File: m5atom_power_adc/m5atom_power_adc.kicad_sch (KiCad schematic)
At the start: 47 parts, among them J1 USB_C_Receptacle_USB2.0_14P, U1 LM2596S-5, U2 ESP32-S3-MINI-1, U3 AMS1117-3.3, U4 ADS1115IDGS, U5 AMS1117-3.3

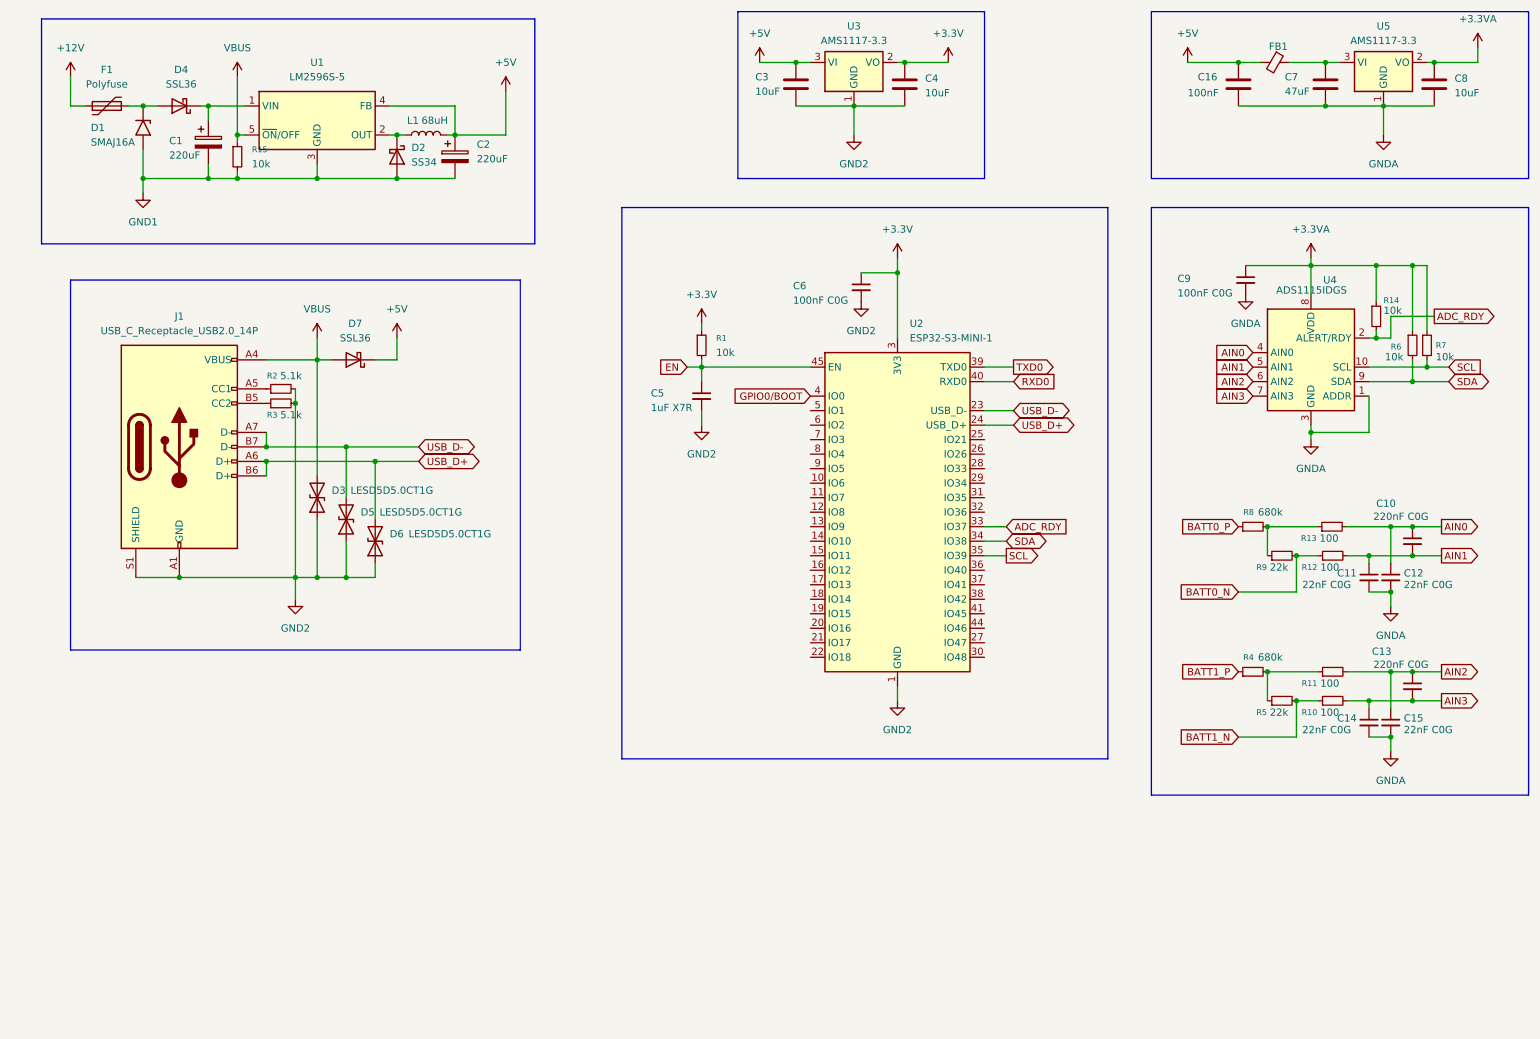
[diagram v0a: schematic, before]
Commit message: fix: 必須な外部接続系を追加
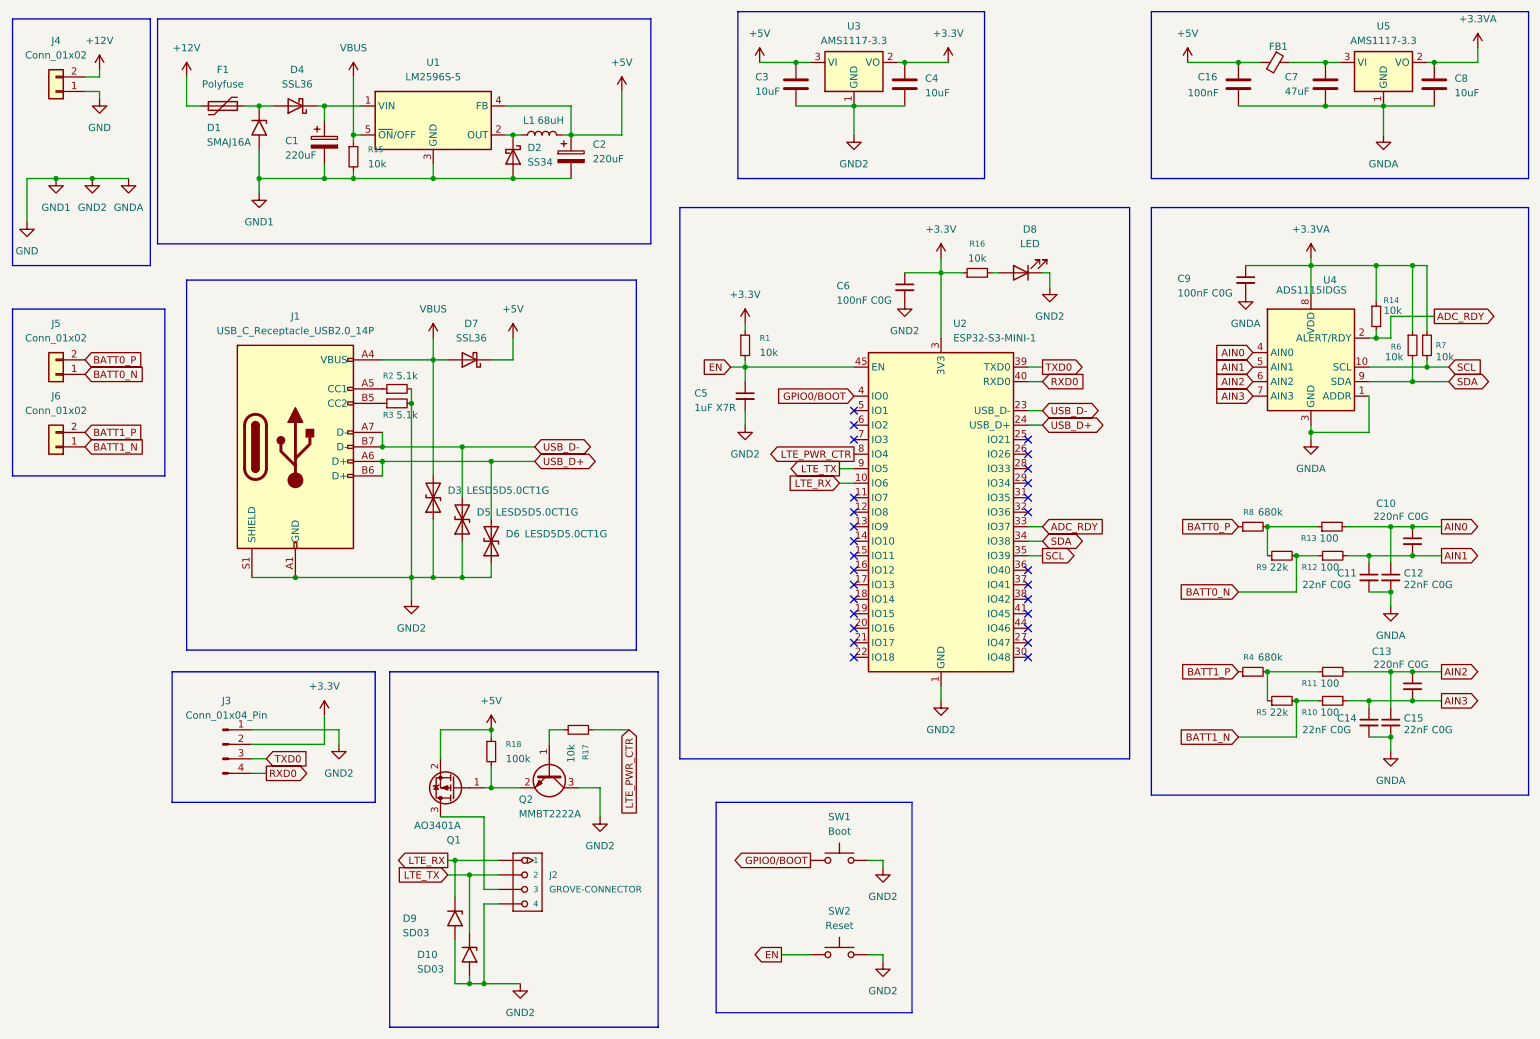
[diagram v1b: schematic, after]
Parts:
- added D10, D9: SD03, Diode_SMD:D_SMA, symbol Diode:SMAJ16A
- added D8: LED, symbol Device:LED
- added J2: GROVE-CONNECTOR, symbol OPL_Connector:GROVE-CONNECTOR-DIP_4P-2.0_
- added J3: Conn_01x04_Pin, symbol Connector:Conn_01x04_Pin
- added J4, J5, J6: Conn_01x02, symbol Connector_Generic:Conn_01x02
- added Q1: AO3401A, Package_TO_SOT_SMD:SOT-23, symbol Transistor_FET:AO3401A
- added Q2: MMBT2222A, Package_TO_SOT_SMD:SOT-23, symbol Transistor_BJT:MMBT2222A
- added R16, R17: 10k, symbol Device:R_Small
- added R18: 100k, symbol Device:R_Small
- added SW1: Boot, symbol Switch:SW_Push
- added SW2: Reset, symbol Switch:SW_Push
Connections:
- net GND2 is gone; now on net GND: C3.2, C4.2, C5.2, C6.2, D3.1 (A1), D5.1 (A1), D6.1 (A1), J1.A1 (GND), J1.A12 (GND), J1.B1 (GND), J1.B12 (GND), J1.S1 (SHIELD), R2.2, R3.2, U2.1 (GND), U2.2 (GND), U2.42 (GND), U2.43 (GND), U2.46 (GND), U2.47 (GND), U2.48 (GND), U2.49 (GND), U2.50 (GND), U2.51 (GND), U2.52 (GND), U2.53 (GND), U2.54 (GND), U2.55 (GND), U2.56 (GND), U2.57 (GND), U2.58 (GND), U2.59 (GND), U2.60 (GND), U2.61 (GND), U2.62 (GND), U2.63 (GND), U2.64 (GND), U2.65 (GND), U3.1 (GND)
- net GNDA is gone; now on net GND: C11.2, C12.2, C14.2, C15.2, C16.2, C7.2, C8.2, C9.2, U4.1 (ADDR), U4.3 (GND), U5.1 (GND)
- net +12V: now also J4.2 (Pin_2)
- net +3.3V: now also J3.2 (Pin_2), R16.1
- net +5V: now also Q1.2 (S), R18.1
- net BATT0_N: now also J5.1 (Pin_1)
- net BATT0_P: now also J5.2 (Pin_2)
- net BATT1_N: now also J6.1 (Pin_1)
- net BATT1_P: now also J6.2 (Pin_2)
- net EN: now also SW2.1
- net GPIO0/BOOT: now also SW1.1
- net RXD0: now also J3.4 (Pin_4)
- net TXD0: now also J3.3 (Pin_3)
- net LTE_RX: now reaches U2.10 (IO6)
- net LTE_RX: now also D9.1 (A1), J2.1
- net LTE_PWR_CTR: now reaches U2.8 (IO4)
- net LTE_PWR_CTR: now also R17.1
- net LTE_TX: now reaches U2.9 (IO5)
- net LTE_TX: now also D10.1 (A1), J2.2
- net GND1 renamed GND
- net GND: now also D10.2 (A2), D8.1 (K), D9.2 (A2), J2.4, J3.1 (Pin_1), J4.1 (Pin_1), Q2.3 (C), SW1.2, SW2.2
- new net: Q1.1 (G), Q2.2 (E), R18.2
- new net: J2.3, Q1.3 (D)
- new net: Q2.1 (B), R17.2
- new net: D8.2 (A), R16.2
- no-connect marks 0 -> 28
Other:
- moved on the sheet: C1, C2, C5, C6, D1, D2, D3, D4, D5, D6, D7, F1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

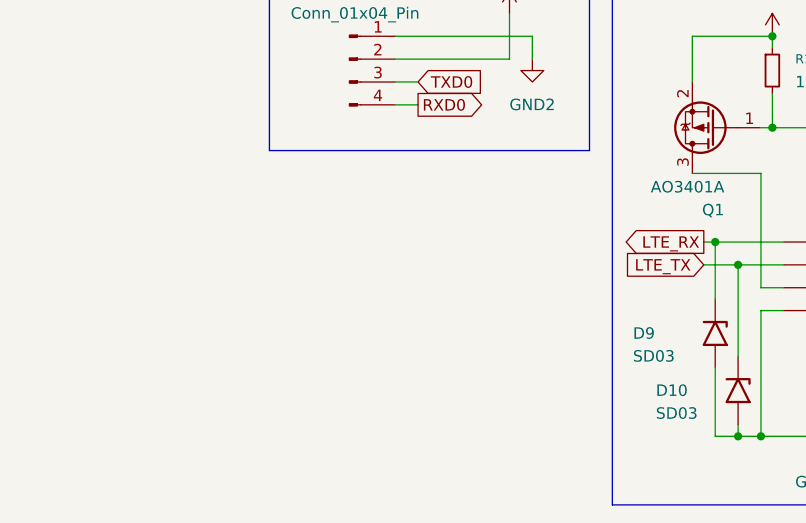
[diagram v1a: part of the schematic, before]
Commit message: fix: リレー駆動用回路テンプレ追加
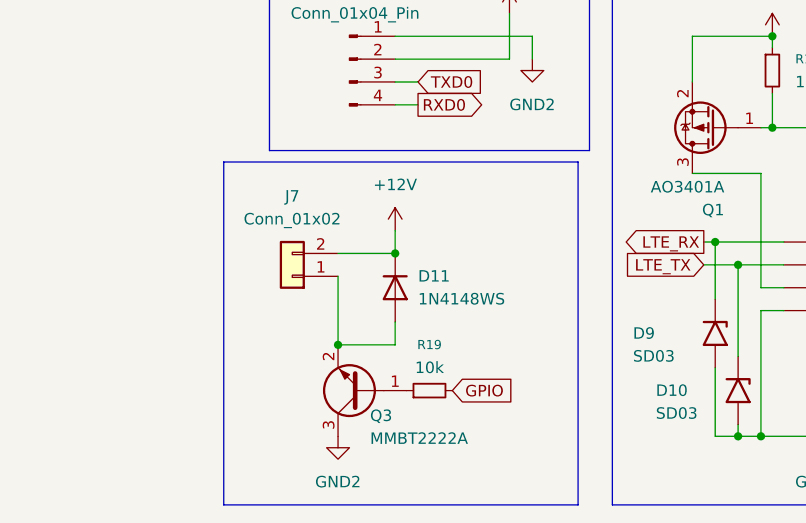
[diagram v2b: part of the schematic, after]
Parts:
- added D11: 1N4148WS, Diode_SMD:D_SOD-323, symbol Diode:1N4148WS
- added J7: Conn_01x02, symbol Connector_Generic:Conn_01x02
- added Q3: MMBT2222A, Package_TO_SOT_SMD:SOT-23, symbol Transistor_BJT:MMBT2222A
- added R19: 10k, symbol Device:R_Small
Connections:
- net +12V: now also D11.1 (K), J7.2 (Pin_2)
- net GND: now also Q3.3 (C)
- new net: D11.2 (A), J7.1 (Pin_1), Q3.2 (E)
- new net: Q3.1 (B), R19.1
- new net GPIO: R19.2

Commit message: fix: いろいろ更新
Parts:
- added D12: 1N4148WS, Diode_SMD:D_SOD-323, symbol Diode:1N4148WS
- added J8: Conn_01x02, symbol Connector_Generic:Conn_01x02
- added Q4: MMBT2222A, Package_TO_SOT_SMD:SOT-23, symbol Transistor_BJT:MMBT2222A
- added R20: 1k, symbol Device:R_Small
- C1: footprint (none) -> Capacitor_SMD:CP_Elec_10x10; JLC (none) -> C125976; JLC_Num (none) -> C125976
- C16: value 100nF -> 100nF C0G; footprint (none) -> Capacitor_SMD:C_1206_3216Metric; JLC_Num (none) -> C2168319
- C2: footprint (none) -> Capacitor_SMD:CP_Elec_10x10; JLC_Num (none) -> C125976
- C6, C9: footprint (none) -> Capacitor_SMD:C_1206_3216Metric; JLC_Num (none) -> C2168319
- D1: footprint Diode_SMD:D_SMA -> Diode_SMD:D_SMB; JLC_Num (none) -> C19077571
- D10, D9: footprint Diode_SMD:D_SMA -> Diode_SMD:D_SOD-323; JLC_Num (none) -> C502526
- D11: JLC_Num (none) -> C2128
- D2: JLC_Num (none) -> C8678
- D4, D7: footprint (none) -> Diode_SMD:D_SMA; JLC_Num (none) -> C28646286
- R19: value 10k -> 1k
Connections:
- net +12V: now also C1.1, D4.1 (K), U1.1 (VIN), D12.1 (K), J8.2 (Pin_2); no longer F1.1, J4.2 (Pin_2)
- net GND: now also Q4.3 (C)
- net LTE_PWR_CTR: no longer U2.8 (IO4)
- net GPIO renamed Relay0
- new net: Q4.1 (B), R20.1
- new net: D12.2 (A), J8.1 (Pin_1), Q4.2 (E)
- new net +BATT: F1.1, J4.2 (Pin_2)
- new net Relay1: R20.2
- no-connect marks 28 -> 30
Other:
- moved on the sheet: C1, C10, C11, C12, C13, C14, C15, C16, C2, C3, C4, C5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

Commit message: feat: 回路図完成？BOM更新中
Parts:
- added D13, D14: SD03, Diode_SMD:D_SOD-323, symbol Diode:SMAJ16A
- added D15, D16, D18: LED, symbol Device:LED
- added D17: 1N4148WS, Diode_SMD:D_SOD-323, symbol Diode:1N4148WS
- added J10: Conn_01x02, symbol Connector_Generic:Conn_01x02
- added J9: GROVE-CONNECTOR, symbol OPL_Connector:GROVE-CONNECTOR-DIP_4P-2.0_
- added Q5: AO3401A, Package_TO_SOT_SMD:SOT-23, symbol Transistor_FET:AO3401A
- added Q6, Q7: MMBT2222A, Package_TO_SOT_SMD:SOT-23, symbol Transistor_BJT:MMBT2222A
- added R21, R27, R29, R31: 100k, symbol Device:R_Small
- added R22: 10k, symbol Device:R_Small
- added R23, R24, R26: 5.1k, symbol Device:R_Small
- added R25: 1k, symbol Device:R_Small
- added R28, R30, R32: 27k, symbol Device:R_Small
- added TP1, TP2, TP3, TP4, TP5, TP6, TP7, TP8: TestPoint, TestPoint:TestPoint_Pad_D1.5mm, symbol Connector:TestPoint
- C10, C13: footprint (none) -> Capacitor_SMD:C_1206_3216Metric; JLC_Num (none) -> C464977
- C11, C12, C14, C15: footprint (none) -> Capacitor_SMD:C_0805_2012Metric; JLC_Num (none) -> C77069
- C3, C4, C8: footprint (none) -> Capacitor_SMD:C_0805_2012Metric; JLC_Num (none) -> C32635
- C5: footprint (none) -> Capacitor_SMD:C_0603_1608Metric; JLC_Num (none) -> C5199872
- C7: value 47uF -> 10uF; footprint (none) -> Capacitor_SMD:C_0805_2012Metric; JLC_Num (none) -> C32635
- D3, D5, D6: footprint (none) -> Diode_SMD:D_SOD-523; JLC_Num (none) -> C5199850
- R16: value 10k -> 1k
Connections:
- net LTE_PWR_CTR is gone; now on net LTE_EN: R17.1
- net +12V: now also D17.1 (K), J10.2 (Pin_2), R23.2, R24.2, R26.2, TP1.1
- net +3.3V: now also J3.1 (Pin_1), TP3.1; no longer J3.2 (Pin_2), R16.1
- net +3.3VA: now also TP4.1
- net +5V: now also R16.1, Q5.2 (S), R21.1, TP2.1
- net ADC_RDY: now also U2.13 (IO9); no longer U2.33 (IO37)
- net AIN0: now also TP7.1
- net AIN2: now also TP8.1
- net GND: now also J3.2 (Pin_2), D13.2 (A2), D14.2 (A2), J9.4, Q6.3 (C), Q7.3 (C), R28.2, R30.2, R32.2, TP5.1, TP6.1; no longer J3.1 (Pin_1)
- net Relay0: now also U2.14 (IO10)
- net Relay1: now also U2.15 (IO11)
- net SCL: now also U2.11 (IO7); no longer U2.35 (IO39)
- net SDA: now also U2.12 (IO8); no longer U2.34 (IO38)
- net at D11.2 (A), J7.1 (Pin_1), Q3.2 (E): now also D16.1 (K), R31.1
- net at D12.2 (A), J8.1 (Pin_1), Q4.2 (E): now also D15.1 (K), R29.1
- net Relay2: now reaches U2.16 (IO12)
- net Relay2: now also R25.2
- net Relay0Sense: now reaches U2.17 (IO13)
- net Relay0Sense: now also R31.2, R32.1
- net Relay1Sense: now reaches U2.18 (IO14)
- net Relay1Sense: now also R29.2, R30.1
- net Relay2Sense: now reaches U2.19 (IO15)
- net Relay2Sense: now also R27.2, R28.1
- net Res0_EN: now reaches U2.20 (IO16)
- net Res0_EN: now also R22.1
- net Res0_0: now reaches U2.21 (IO17)
- net Res0_0: now also D14.1 (A1), J9.2
- net Res0_1: now reaches U2.22 (IO18)
- net Res0_1: now also D13.1 (A1), J9.1
- net LTE_EN: now reaches U2.8 (IO4)
- new net: D17.2 (A), D18.1 (K), J10.1 (Pin_1), Q7.2 (E), R27.1
- new net: Q6.1 (B), R22.2
- new net: Q5.1 (G), Q6.2 (E), R21.2
- new net: Q7.1 (B), R25.1
- new net: D18.2 (A), R26.1
- new net: D16.2 (A), R24.1
- new net: J9.3, Q5.3 (D)
- new net: D15.2 (A), R23.1
- no-connect marks 30 -> 19
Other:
- moved on the sheet: C3, C4, D10, D11, D12, D3, D5, D6, D7, D8, D9, J1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
